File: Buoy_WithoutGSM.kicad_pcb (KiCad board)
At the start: 2 copper layers, 44.2 x 102.4 mm, 15 parts, among them J1 Conn_Battery_JST, J2 Conn_Battery_Terminal_Block, J3 Conn_DC_Motor_A, J4 Conn_DC_Motor_B, J5 Conn_Servo, J6 Conn_VCC_ESP32, J7 Conn_Extras, U1 Ultimate_GPS, U2 ESP32-DEVKITC-32D, U3 RFM95W_Board, U5 TB6612FNG

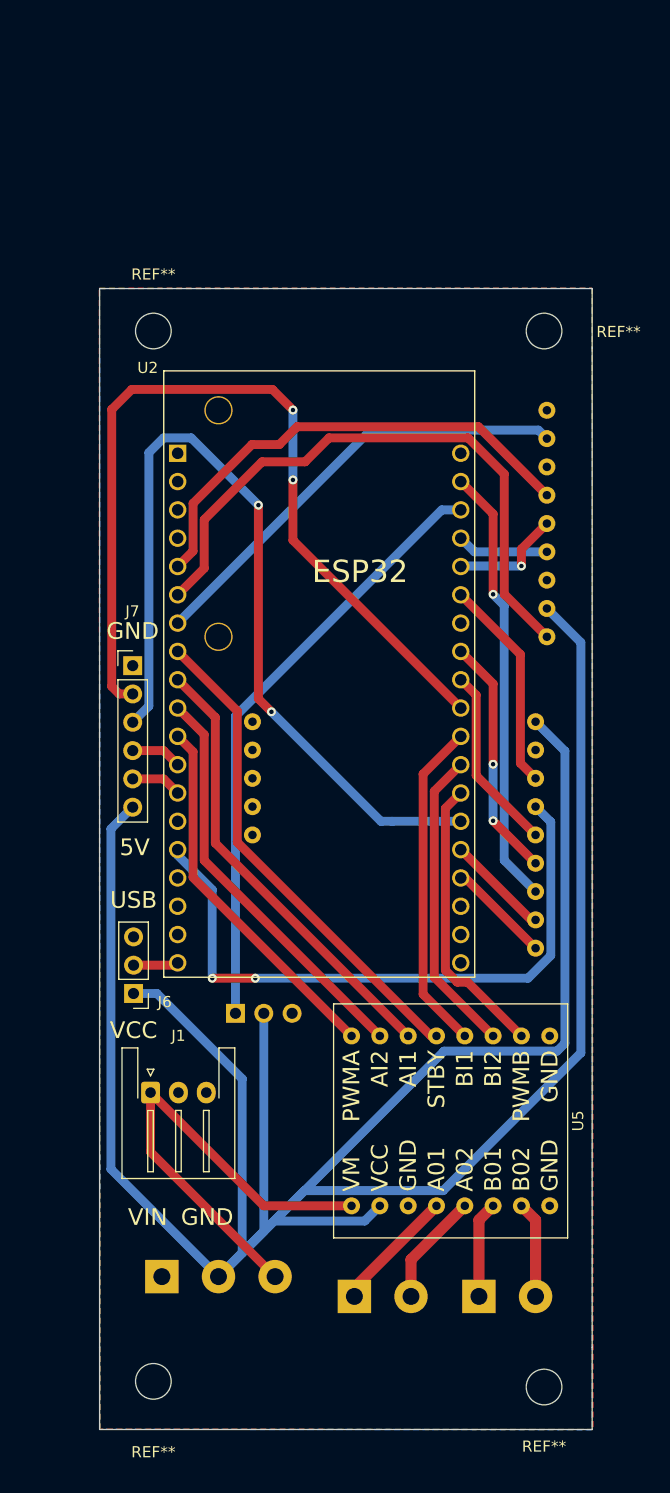
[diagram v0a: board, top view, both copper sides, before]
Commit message: Added 3D model for the Ethernet module and routed changes on PCB
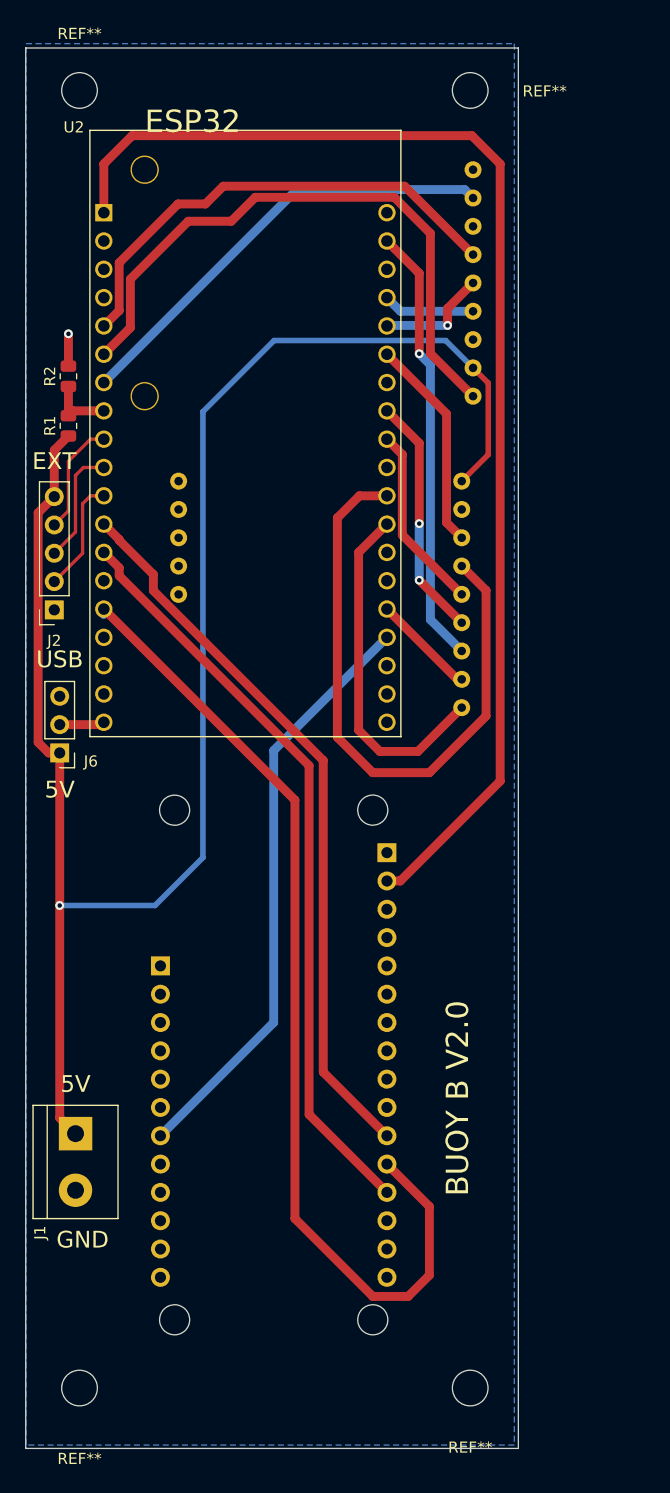
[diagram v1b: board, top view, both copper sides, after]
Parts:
- removed J3: Conn_DC_Motor_A, TerminalBlock:TerminalBlock_bornier-2_P5.08mm
- removed J4: Conn_DC_Motor_B, TerminalBlock:TerminalBlock_bornier-2_P5.08mm
- removed J5: Conn_Servo, Connector_PinHeader_2.54mm:PinHeader_1x03_P2.54mm_Vertical
- removed J7: Conn_Extras, Connector_PinHeader_2.54mm:PinHeader_1x06_P2.54mm_Vertical
- removed the REF** at (173.5, 58.2)
- removed the REF** at (138.4, 58.2)
- removed the REF** at (173.5, 152.9)
- removed U5: TB6612FNG, Footprints:TB6612FNG
- added R1: 10K, Resistor_SMD:R_0805_2012Metric, F.Cu at (130.8, 66.7)
- added R2: 10K, Resistor_SMD:R_0805_2012Metric, F.Cu at (130.8, 62.2)
- added REF**: MountingHole_3.2mm_M3, MountingHole:MountingHole_3.2mm_M3, F.Cu at (166.9, 36.6)
- added REF**: MountingHole_3.2mm_M3, MountingHole:MountingHole_3.2mm_M3, F.Cu at (131.8, 36.6)
- added REF**: MountingHole_3.2mm_M3, MountingHole:MountingHole_3.2mm_M3, F.Cu at (166.9, 153.0)
- added U4: Ethernet-FeatherWing, Ethernet-FeatherWing:Ethernet FeatherWing, B.Cu at (139.1, 121.5)
- J1: value Conn_Battery_JST -> Conn_01x02_Female; footprint Connector_JST:JST_XH_S3B-XH-A-1_1x03_P2.50mm_Horizontal -> TerminalBlock:TerminalBlock_bornier-2_P5.08mm
- J2: value Conn_Battery_Terminal_Block -> Conn_01x05_Male; footprint TerminalBlock:TerminalBlock_bornier-3_P5.08mm -> Connector_PinSocket_2.54mm:PinSocket_1x05_P2.54mm_Vertical; moved to F.Cu
- moved J2 60.6 mm to (129.5, 83.2), turned to 180 degrees
- moved J6 22.6 mm to (130.0, 96.0)
- moved U1 22.6 mm to (152.1, 53.9)
- moved U2 22.6 mm to (146.7, 67.3)
- moved U3 22.6 mm to (153.4, 81.8)
- moved J1 7.67 mm to (131.4, 130.2), turned to -90 degrees
- moved REF** 6.65 mm to (131.8, 153.0)
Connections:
- J1 pad 1: VIN -> 5V
- J1 pad 2: Net-(J1-Pad2) -> GND
- J2 pad 2: 5V -> IO27_ESP
- J2 pad 3: VIN -> IO26_ESP
- J6 pad 3: Net-(J6-Pad3) -> unconnected-(J6-Pad3)
- U1 pad 1: Net-(U1-Pad1) -> unconnected-(U1-Pad1)
- U1 pad 3: Net-(U1-Pad3) -> unconnected-(U1-Pad3)
- U2 pad 1: Net-(U2-Pad1) -> 3V3
- U2 pad 10: AIN2_TB6612FNG -> IO26_ESP
- U2 pad 11: PWMA_TB6612FNG -> IO27_ESP
- U2 pad 12: Net-(J7-Pad4) -> SCK_ETHERNET
- U2 pad 13: Net-(J7-Pad5) -> MISO_ETHERNET
- U2 pad 15: IRQ_RFM95W -> MOSI_ETHERNET
- U2 pad 16: Net-(U2-Pad16) -> unconnected-(U2-Pad16)
- U2 pad 17: Net-(U2-Pad17) -> unconnected-(U2-Pad17)
- U2 pad 18: Net-(U2-Pad18) -> unconnected-(U2-Pad18)
- U2 pad 2: Net-(U2-Pad2) -> unconnected-(U2-Pad2)
- U2 pad 22: PWM_Servo -> unconnected-(U2-Pad22)
- U2 pad 29: IO0_ESP -> unconnected-(U2-Pad29)
- U2 pad 3: Net-(U2-Pad3) -> unconnected-(U2-Pad3)
- U2 pad 30: BIN1_TB6612FNG -> IRQ_RFM95W
- U2 pad 31: BIN2_TB6612FNG -> RST_RFM95W
- U2 pad 32: PWMB_TB6612FNG -> unconnected-(U2-Pad32)
- U2 pad 33: IO5_ESP -> unconnected-(U2-Pad33)
- U2 pad 35: RST_RFM95W -> CS_ETHERNET
- U2 pad 36: Net-(U2-Pad36) -> unconnected-(U2-Pad36)
- U2 pad 37: Net-(U2-Pad37) -> unconnected-(U2-Pad37)
- U2 pad 38: Net-(U2-Pad38) -> unconnected-(U2-Pad38)
- U2 pad 4: Net-(U2-Pad4) -> unconnected-(U2-Pad4)
- U2 pad 8: STBY_TB6612FNG -> INPUT-MEASURE
- U2 pad 9: AIN1_TB6612FNG -> IO25_ESP
- U3 pad 10: Net-(U3-Pad10) -> unconnected-(U3-Pad10)
- U3 pad 11: Net-(U3-Pad11) -> unconnected-(U3-Pad11)
- U3 pad 12: Net-(U3-Pad12) -> unconnected-(U3-Pad12)
- U3 pad 13: Net-(U3-Pad13) -> unconnected-(U3-Pad13)
- U3 pad 14: Net-(U3-Pad14) -> unconnected-(U3-Pad14)
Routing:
- net 5V: track 272.5 -> 159.9 mm, vias 0 -> 1
- net 3V3: track 0.00 -> 111.3 mm
- net MOSI_ETHERNET: track 0.00 -> 89.6 mm
- net IO0_ESP: track 77.8 -> 0.00 mm, vias 2 -> 0
- net IO5_ESP: track 77.8 -> 0.00 mm, vias 2 -> 0
- net MISO_ETHERNET: track 0.00 -> 67.9 mm
- net SCK_ETHERNET: track 0.00 -> 65.4 mm
- net PWM_Servo: track 54.5 -> 0.00 mm
- net CS_ETHERNET: track 0.00 -> 53.5 mm
- net STBY_TB6612FNG: track 44.4 -> 0.00 mm
- net VIN: track 43.4 -> 0.00 mm
- net AIN1_TB6612FNG: track 40.5 -> 0.00 mm
- net AIN2_TB6612FNG: track 36.9 -> 0.00 mm
- net PWMA_TB6612FNG: track 33.3 -> 0.00 mm
- net BIN1_TB6612FNG: track 29.8 -> 0.00 mm
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- removed copper zone on F.Cu, net GND
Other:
- board size 44.2 x 102.4 mm -> 44.2 x 125.6 mm
- net class Default removed
- board text added: "BUOY B V2.0"
- board text added: "EXT"
- board text added: "Ethernet FeatherWing"
- board text added: "LoRa RFM95W"
- board text removed: "A01"
- board text removed: "A02"
- board text removed: "B01"
- board text removed: "B02"
- board text removed: "EJA - BUOY B V1.0"
- board text removed: "L.W. E.K. O.O."
- board text removed: "LoRa_RFM95W"
- board text removed: "PMW"
- board text removed: "VCC"
- board text removed: "VIN"

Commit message: Changed toutes of the PCB, including routes width
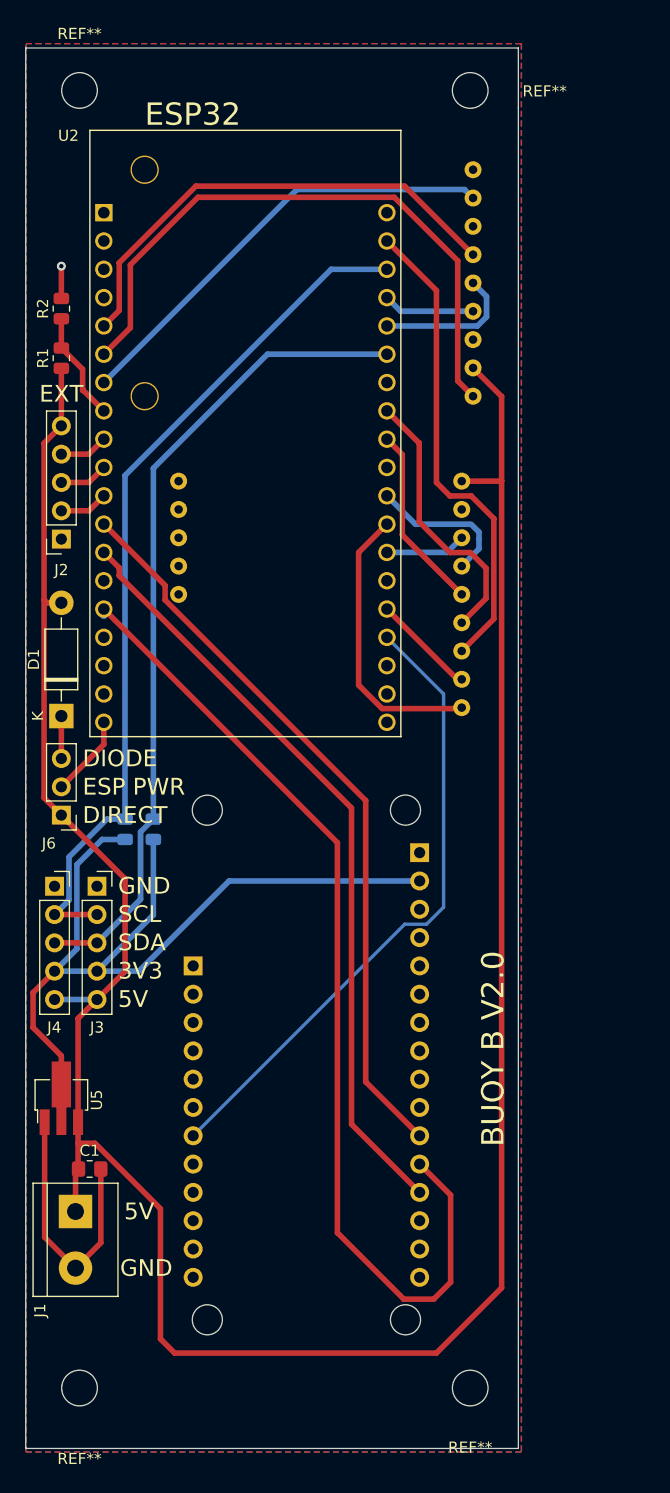
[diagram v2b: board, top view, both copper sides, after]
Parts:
- added C1: 47uF, Resistor_SMD:R_0805_2012Metric_Pad1.20x1.40mm_HandSolder, F.Cu at (132.7, 133.3)
- added D1: 1N5818, Diode_THT:D_DO-41_SOD81_P10.16mm_Horizontal, F.Cu at (130.2, 92.7)
- added J3: Conn_01x05_Male, Connector_PinSocket_2.54mm:PinSocket_1x05_P2.54mm_Vertical, F.Cu at (133.4, 108.0)
- added J4: Conn_01x05_Male, Connector_PinSocket_2.54mm:PinSocket_1x05_P2.54mm_Vertical, F.Cu at (129.6, 108.0)
- added R3: 10K, Resistor_SMD:R_0805_2012Metric, B.Cu at (138.4, 102.9)
- added R4: 10K, Resistor_SMD:R_0805_2012Metric, B.Cu at (135.9, 102.9)
- added U5: AZ1117CR-3.3TRG1, Package_TO_SOT_SMD:SOT-89-3_Handsoldering, F.Cu at (130.2, 127.0)
- moved J1 6.98 mm to (131.4, 137.2)
- moved J2 6.38 mm to (130.2, 76.8)
- moved R1 6.11 mm to (130.2, 60.6)
- moved R2 6.11 mm to (130.2, 56.2)
- moved J6 5.58 mm to (130.2, 101.6)
- moved U4 2.93 mm to (142.0, 121.5)
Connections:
- J6 pad 3: unconnected-(J6-Pad3) -> Net-(D1-Pad1)
- U2 pad 1: 3V3 -> unconnected-(U2-Pad1)
- U2 pad 22: unconnected-(U2-Pad22) -> SCL
- U2 pad 25: EN_RFM95W -> SDA
- U2 pad 32: unconnected-(U2-Pad32) -> EN_RFM95W
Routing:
- net SCL: track 0.00 -> 77.9 mm
- net SDA: track 0.00 -> 73.7 mm
- net 5V: track 159.9 -> 228.9 mm, vias 1 -> 0
- net IRQ_RFM95W: track 56.1 -> 13.2 mm
- net 3V3: track 111.3 -> 81.0 mm
- net GND: track 2.90 -> 27.0 mm
- net EN_RFM95W: track 19.2 -> 7.25 mm
- net IO26_ESP: track 10.6 -> 4.37 mm
- net IO27_ESP: track 10.2 -> 4.37 mm
- net IO25_ESP: track 10.2 -> 4.37 mm
- net RST_RFM95W: track 31.2 -> 25.7 mm
- net CS_ETHERNET: track 53.5 -> 57.7 mm
- net INPUT-MEASURE: track 5.97 -> 9.88 mm
- net Net-(D1-Pad1): track 0.00 -> 3.81 mm
- net Net-(J6-Pad2): track 4.04 -> 7.66 mm
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- added copper zone on F.Cu, net GND
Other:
- board text added: "3V3"
- board text added: "DIODE"
- board text added: "DIRECT"
- board text added: "ESP PWR"
- board text added: "SCL"
- board text added: "SDA"
- board text removed: "USB"
